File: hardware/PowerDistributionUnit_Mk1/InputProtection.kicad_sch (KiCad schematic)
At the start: 22 parts, among them Q1 NVMFWS1D7N04XMT1G, U2 LM74502HDDFR

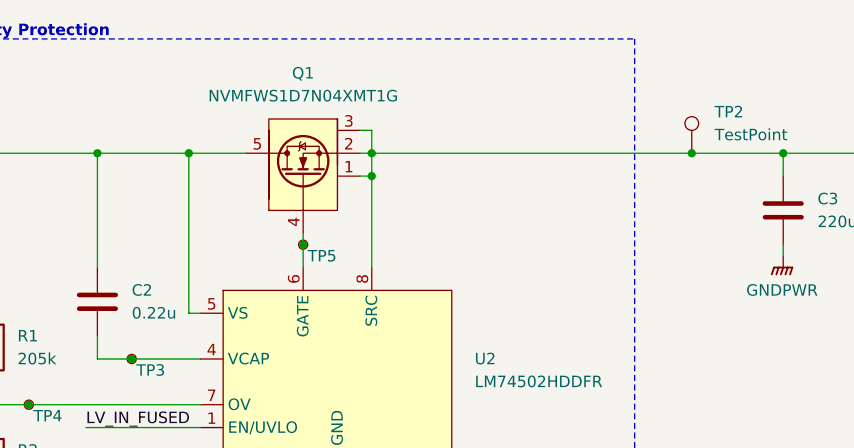
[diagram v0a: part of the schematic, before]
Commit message: BBPDU Mk1 RevB (#6)
* update adc reference to use internal reference (open) with jumper option

* change ADC - reading voltage to resistor divider with option to reference to GND or 1.65V

* change ADC AVDD and AGND connections to regular 3.3V and GND

* make input protection use b2b FETs

* update KiCad-Sharepoint

* update LeaderSOM symbol and SPI pinout (bottom) - need to swap SPI2 and SPI3 names, remove local library copy of LeaderSOM symbol

* change LSOM footprint to centered LSOM footprint, make centered LSOM footprint plated to address hidden pins on LSOM symbol

* update PCB from schematic

* layout/routing for input protection

* fix centered LSOM footprint 3D model, update footprint

* reroute LSOM SPI connections, repin logic analyzer connections

* reroute updated AVDD and AGND on ADCs

* reroute ADCIN- connections to resistor divider from 3.3VA (for 1.65V or 0V)

* change jumper to DNP resistor for ADC reference, routed

* route a couple of missed connections (LV in connection to input prot IC, LV sense connection)

* address DRC

* fix silkscreen labelling issues

* add SRCLK_ENed connection to logic analyzer connector

* silkscreen fixes and stuff

* update rev and year label

* address DRC

* update schematic documentation, clean up, update titleblocks

* add LCSC P/N to libs

* update all symbols with LCSC P/N

* update PCB with LCSC P/Ns

* add center mounting hole

* correct SR part number to SOIC package

* correct fuse table

* change lv sense rdiv values to avoid extended components, update all pull-ups/-downs using 2.8k

* rotate nanofits for inwards clip

* NC the mounting holes (because Lakshay Gupta)

* fix shorted nets error from wrong size res symbol from resistor change

* address DRC

* assembly setup, change latch pull resistor DNP to latch off instead of auto retry by default

* silkscreen stuff

* change DNP for HSS diagnostics to default to current

* change DNP to disable HSS diagnostics by default (primarily use external current 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
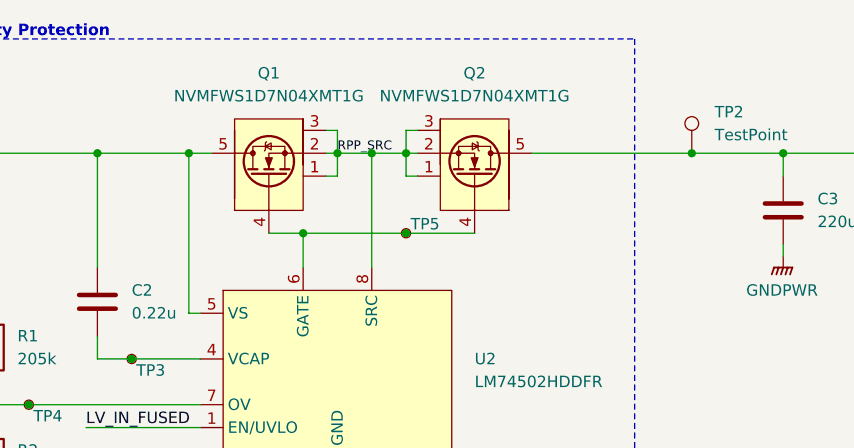
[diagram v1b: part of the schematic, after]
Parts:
- added Q2: NVMFWS1D7N04XMT1G, PowerDistributionUnitLib:NVMFWS1D7N04XMT1G, symbol PowerDistributionUnitLib:NVMFWS1D7N04XMT1G
- C1, C4: LCSC P/N (none) -> C14663
- C100: LCSC P/N (none) -> C57112
- C101, C5: LCSC P/N (none) -> C15849
- C2: LCSC P/N (none) -> C344195
- C3: LCSC P/N (none) -> C2165811
- D1: LCSC P/N (none) -> C1973846
- D34, D35: LCSC P/N (none) -> C5628891
- Q1: Alt LCSC P/N (none) -> C133142
- R1: LCSC P/N (none) -> C22949
- R2: LCSC P/N (none) -> C25804
- R22: LCSC P/N (none) -> C23179
- R23: LCSC P/N (none) -> C22808
- U2: LCSC P/N (none) -> C5219202
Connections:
- net LV: now also Q2.5; no longer Q1.1, Q1.2, Q1.3, U2.8 (SRC)
- net at Q1.4, TP5.1, U2.6 (GATE): now also Q2.4
- new net RPP_SRC: Q1.1, Q1.2, Q1.3, Q2.1, Q2.2, Q2.3, U2.8 (SRC)
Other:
- moved on the sheet: Q1, TP5
